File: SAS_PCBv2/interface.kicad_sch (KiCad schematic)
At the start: 29 parts, among them J10 Conn_01x04, J11 Conn_01x04, J13 Adatateur FTDI (Radio RFD900x), J14 Conn_01x02, J15 Adatateur FTDI (Radio RFD900x), J4 Conn_01x02, J5 Conn_01x02, J6 Conn_01x02, J7 Conn_01x02, J8 Conn_01x02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

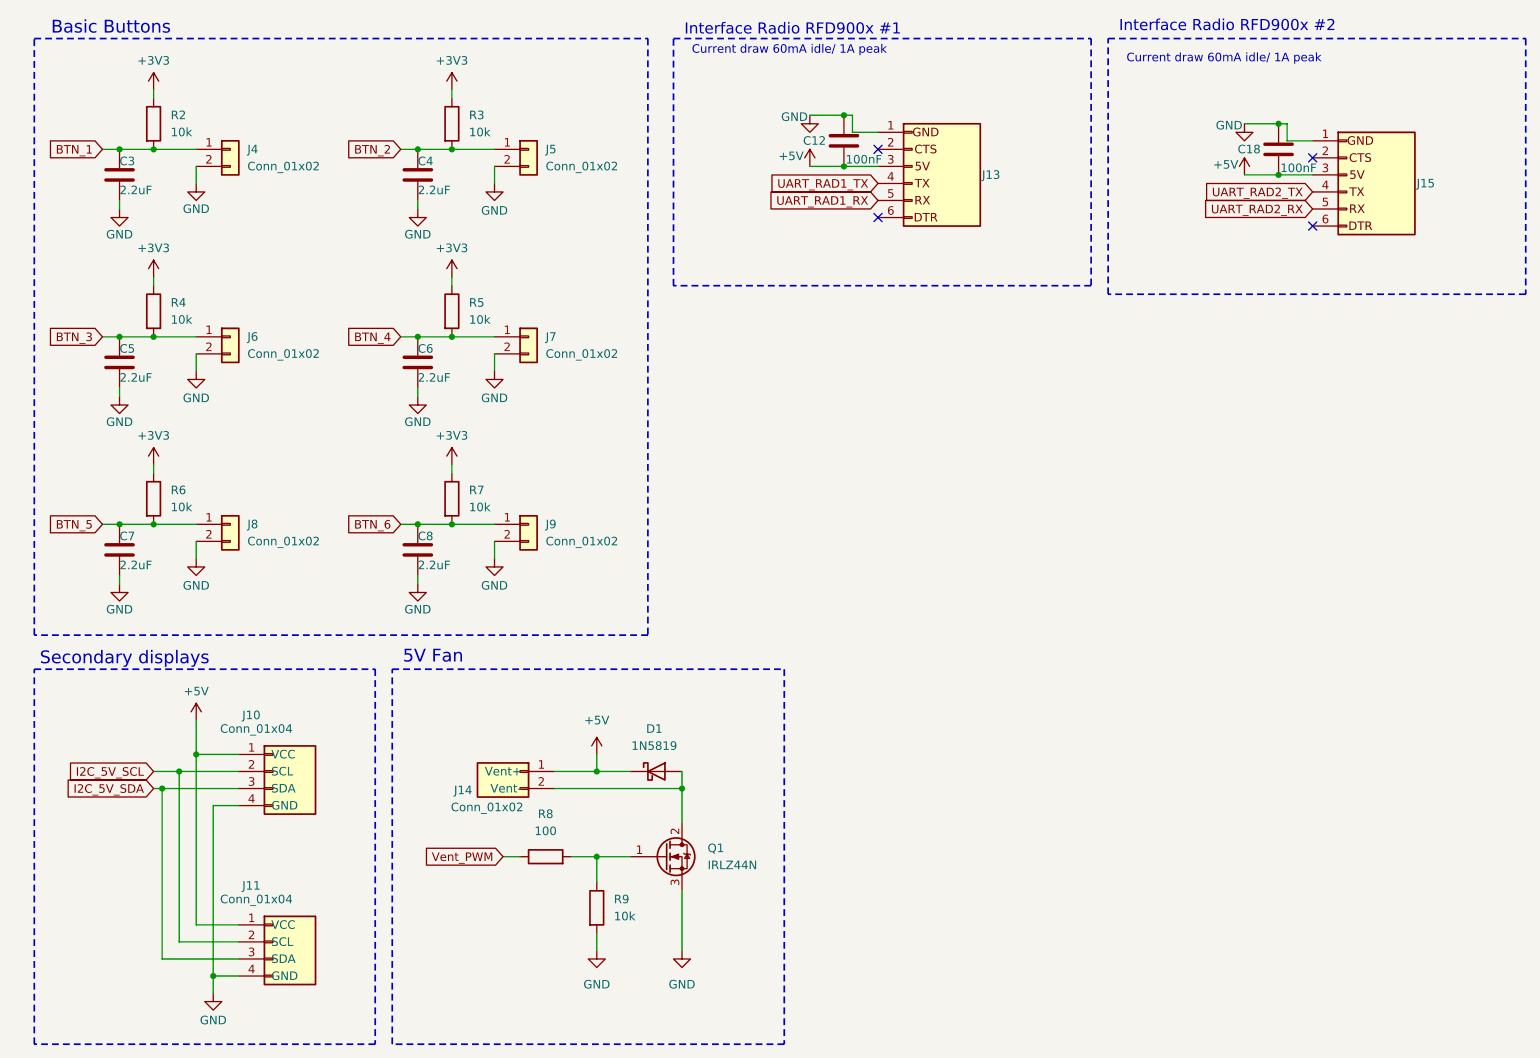
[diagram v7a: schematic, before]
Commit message: Identification des transistors, footprint BMP280 et GPS Neo-6M, correction du fan PWM
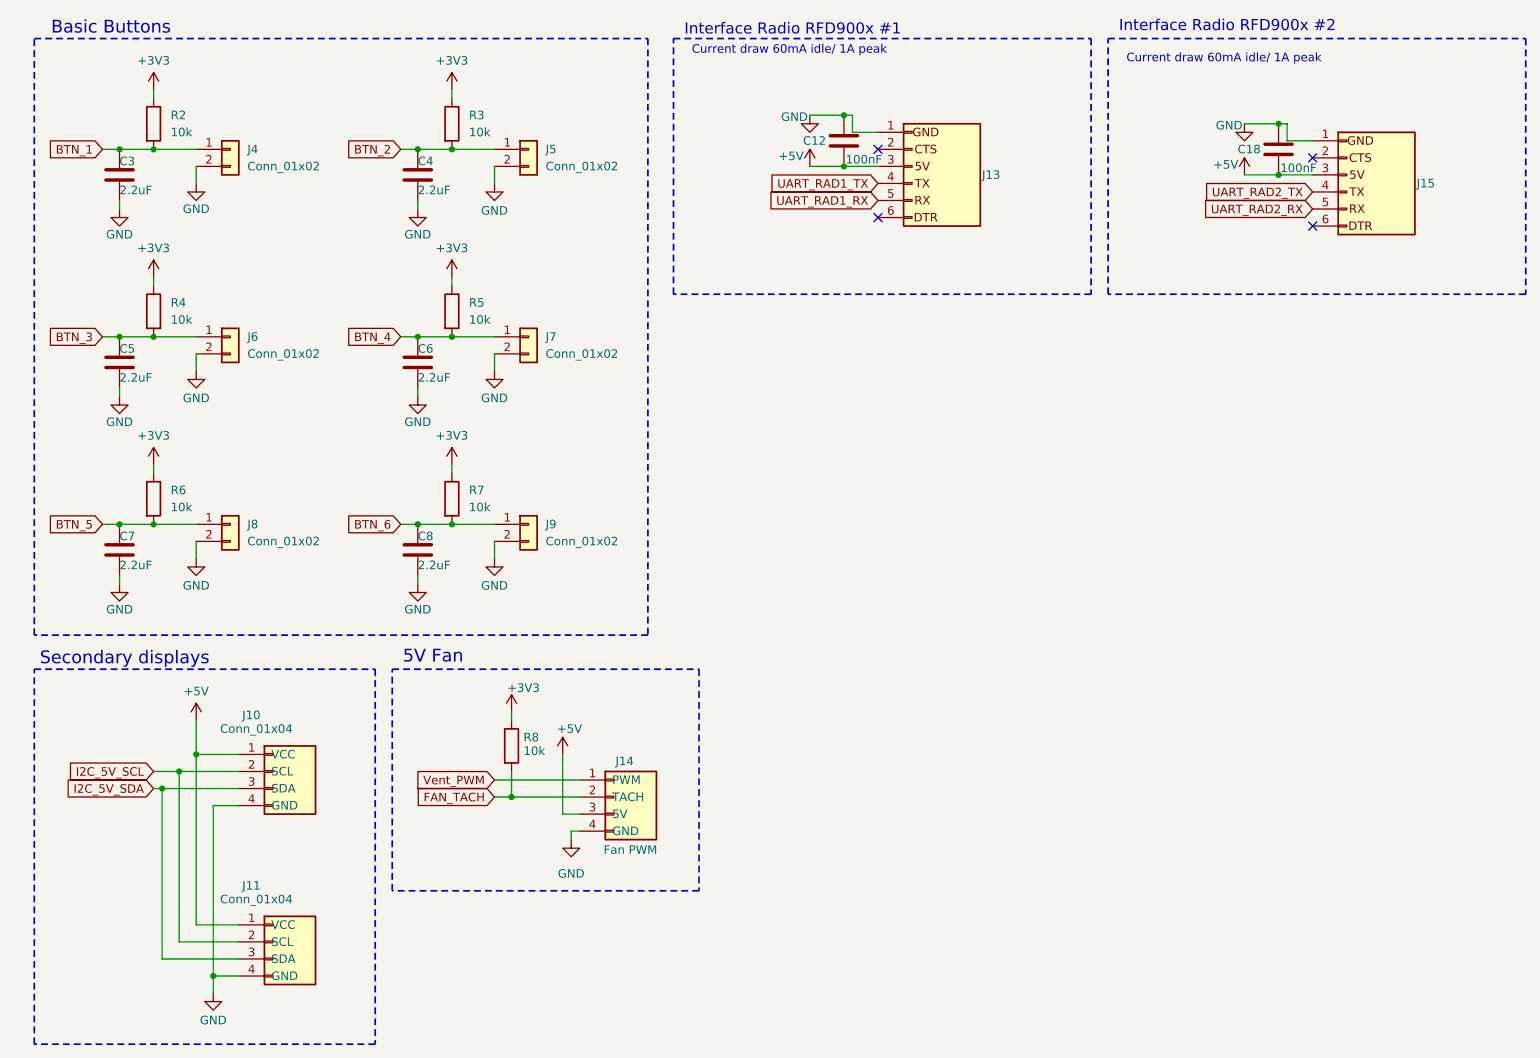
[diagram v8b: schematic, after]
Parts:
- removed D1: 1N5819, Diode_THT:D_DO-41_SOD81_P10.16mm_Horizontal, symbol Diode:1N5819
- removed J14: Conn_01x02, Connector_PinHeader_2.54mm:PinHeader_1x02_P2.54mm_Vertical, symbol Connector_Generic:Conn_01x02
- removed Q1: IRLZ44N, Package_TO_SOT_THT:TO-220-3_Vertical, symbol Transistor_FET:IRLZ44N
- removed R9: 10k, symbol Device:R
- added J14: Fan PWM, symbol Connector_Generic:Conn_01x04
- R8: value 100 -> 10k
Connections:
- net +3V3: now also R8.1
- net +5V: now also J14.3 (5V)
- net GND: now also J14.4 (GND)
- net Vent_PWM: now also J14.1 (PWM); no longer R8.1
- net FAN_TACH: now reaches R8.2
- net FAN_TACH: now also J14.2 (TACH)
